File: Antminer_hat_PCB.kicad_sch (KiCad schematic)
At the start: 36 parts, among them J1 Conn_02x09_Odd_Even, J10 USB Expansion board, J11 Aux_mio_conn, J12 12v Pwr, J13 HDMI_A, J14 PL Pins, J2 Conn_02x09_Odd_Even, J3 Conn_02x09_Odd_Even, J4 Conn_02x09_Odd_Even, J5 Conn_02x09_Odd_Even, J6 Conn_02x09_Odd_Even, J7 Conn_02x09_Odd_Even, J8 Conn_02x09_Odd_Even, J9 Conn_02x09_Odd_Even, U1 L7805

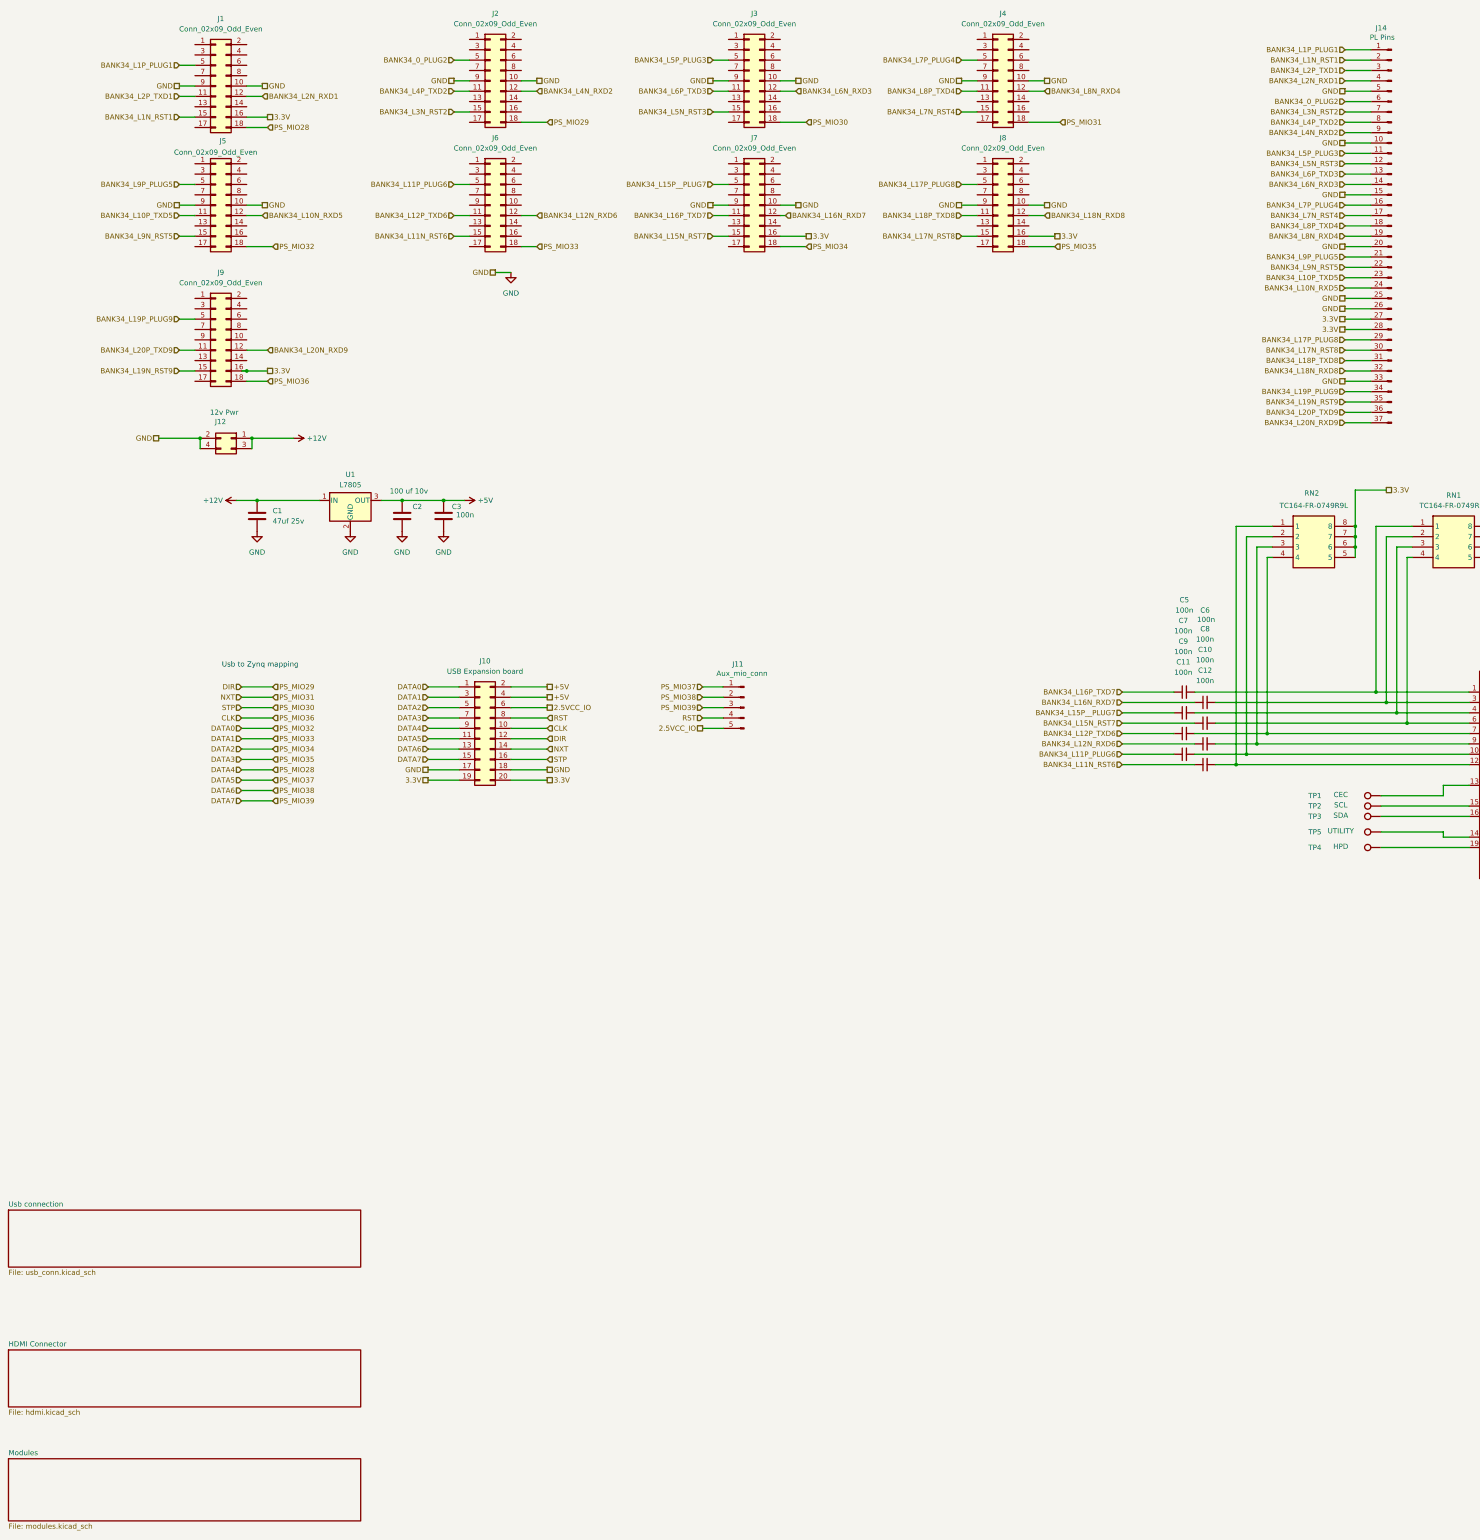
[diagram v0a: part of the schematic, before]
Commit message: Updates for version 1.1:  - Project named as Antminer_hat_pcb  - Added USB3315 Phy on board  - Removed ULPI connector  - Optimized HDMI wiring  - Other updates
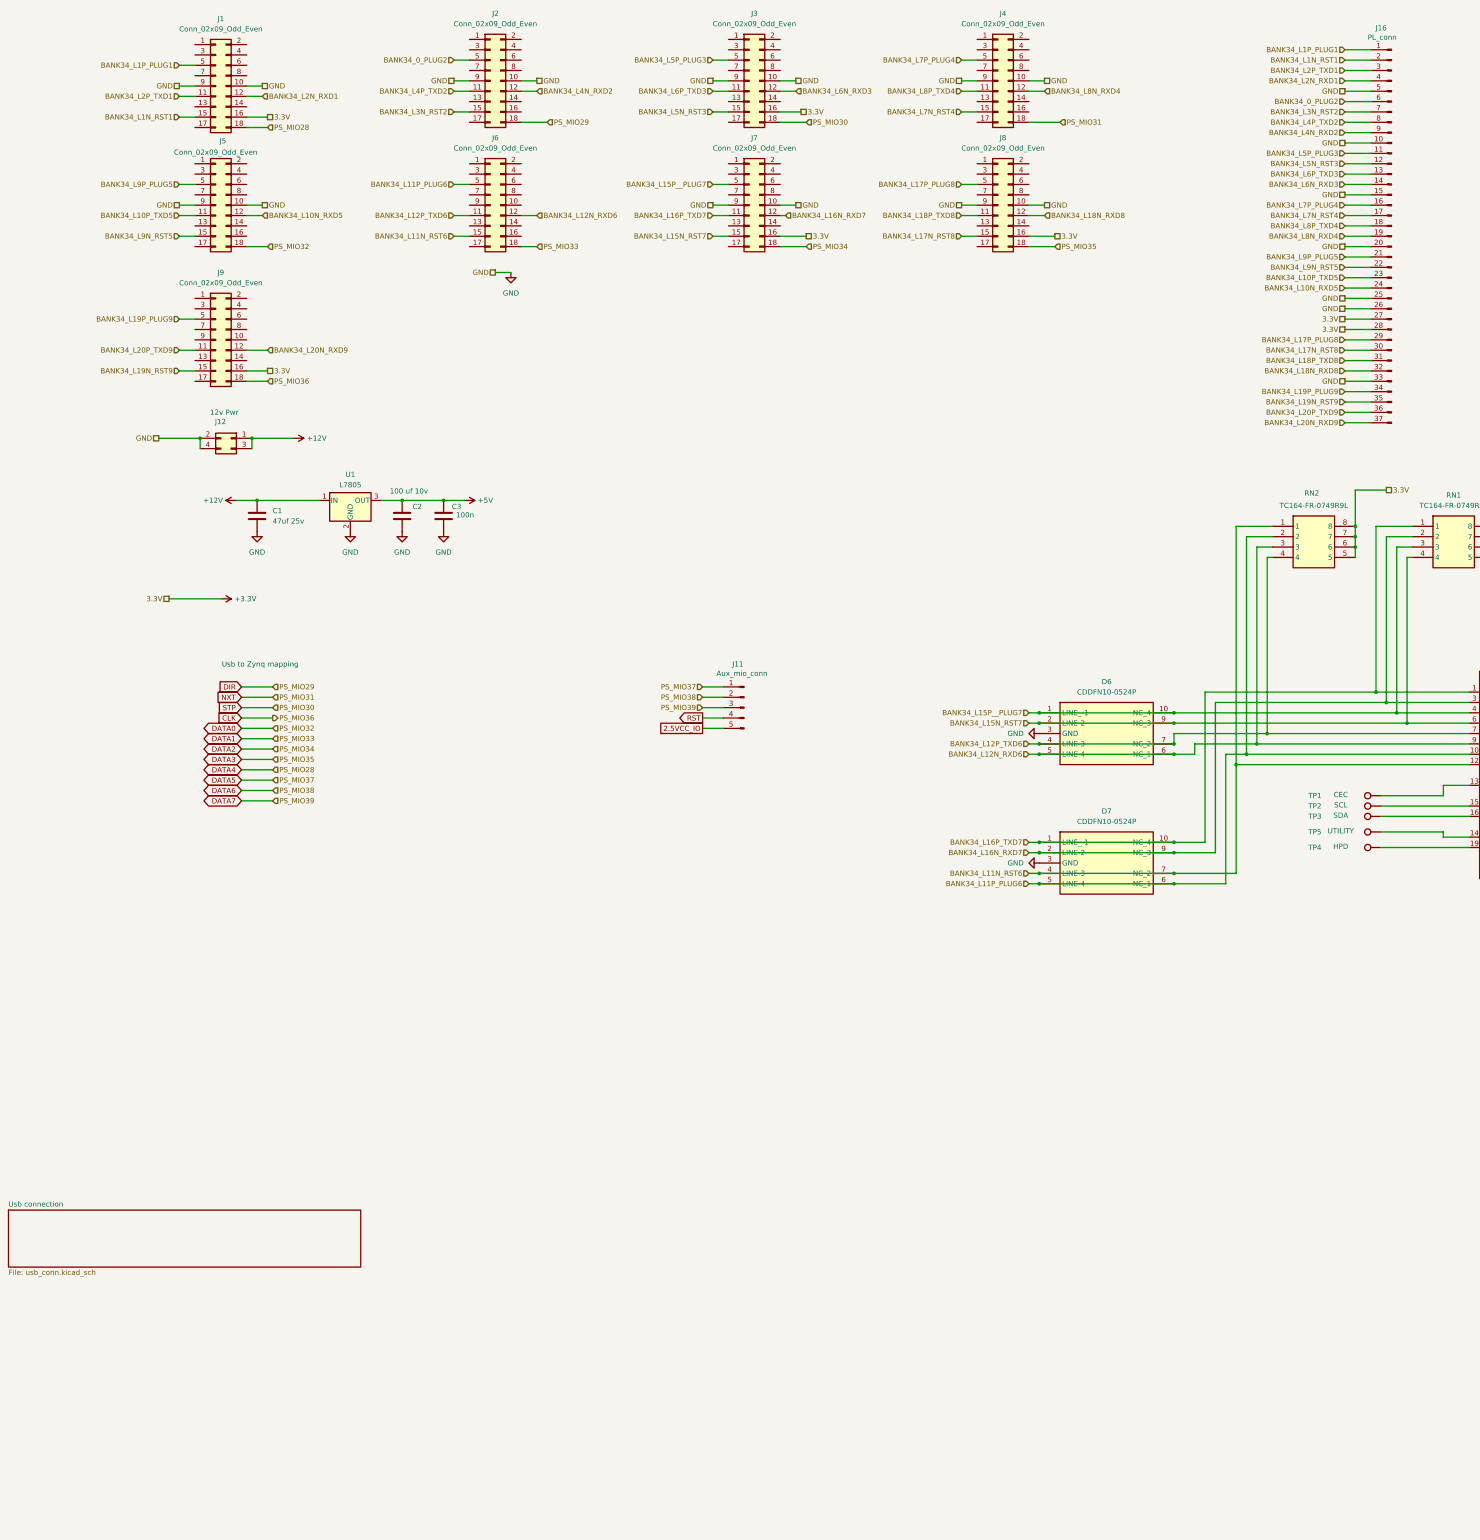
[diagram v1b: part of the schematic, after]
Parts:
- removed C10, C11, C12, C5, C6, C7, C8, C9: 100n, Capacitor_SMD:C_0603_1608Metric_Pad1.08x0.95mm_HandSolder, symbol Device:C_Small
- removed J10: USB Expansion board, Connector_PinSocket_2.54mm:PinSocket_2x10_P2.54mm_Horizontal, symbol Connector_Generic:Conn_02x10_Odd_Even
- added D6, D7: CDDFN10-0524P, SamacSys_Parts:CDDFN100524P, symbol SamacSys_Parts:CDDFN10-0524P
- J16: renamed from J14; value PL Pins -> PL_conn
- R1: footprint Resistor_SMD:R_1206_3216Metric -> Resistor_SMD:R_0805_2012Metric
- TP1, TP2, TP3, TP4, TP5, TP6: footprint TestPoint:TestPoint_Pad_D2.0mm -> TestPoint:TestPoint_Pad_D1.5mm
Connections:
- net 3.3V is gone; now on net +3.3V: J1.16 (Pin_16), J16.27 (Pin_27), J16.28 (Pin_28), J7.16 (Pin_16), J8.16 (Pin_16), J9.16 (Pin_16), RN1.5, RN1.6, RN1.7, RN1.8, RN2.5, RN2.6, RN2.7, RN2.8
- net BANK34_L11N_RST6: now also J13.12 (CK-), RN2.1, D7.4 (LINE-3), D7.7 (NC_2)
- net BANK34_L11P_PLUG6: now also J13.10 (CK+), RN2.2, D7.5 (LINE-4), D7.6 (NC_1)
- net BANK34_L12N_RXD6: now also J13.9 (D0-), RN2.3, D6.5 (LINE-4), D6.6 (NC_1)
- net BANK34_L12P_TXD6: now also J13.7 (D0+), RN2.4, D6.4 (LINE-3), D6.7 (NC_2)
- net BANK34_L15N_RST7: now also J13.6 (D1-), RN1.4, D6.2 (LINE-2), D6.9 (NC_3)
- net BANK34_L15P__PLUG7: now also J13.4 (D1+), RN1.3, D6.1 (LINE_-1), D6.10 (NC_4)
- net BANK34_L16N_RXD7: now also J13.3 (D2-), RN1.2, D7.2 (LINE-2), D7.9 (NC_3)
- net BANK34_L16P_TXD7: now also J13.1 (D2+), RN1.1, D7.1 (LINE_-1), D7.10 (NC_4)
- net GND: now also D6.3 (GND), D7.3 (GND)
- net +3.3V: now reaches J3.16 (Pin_16)
- net PS_MIO30 renamed STP
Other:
- removed sheet HDMI Connector
- removed sheet Modules
- title: KCC Tech S9 Board hat 2025 -> KCC Tech hat board for Antminer S9

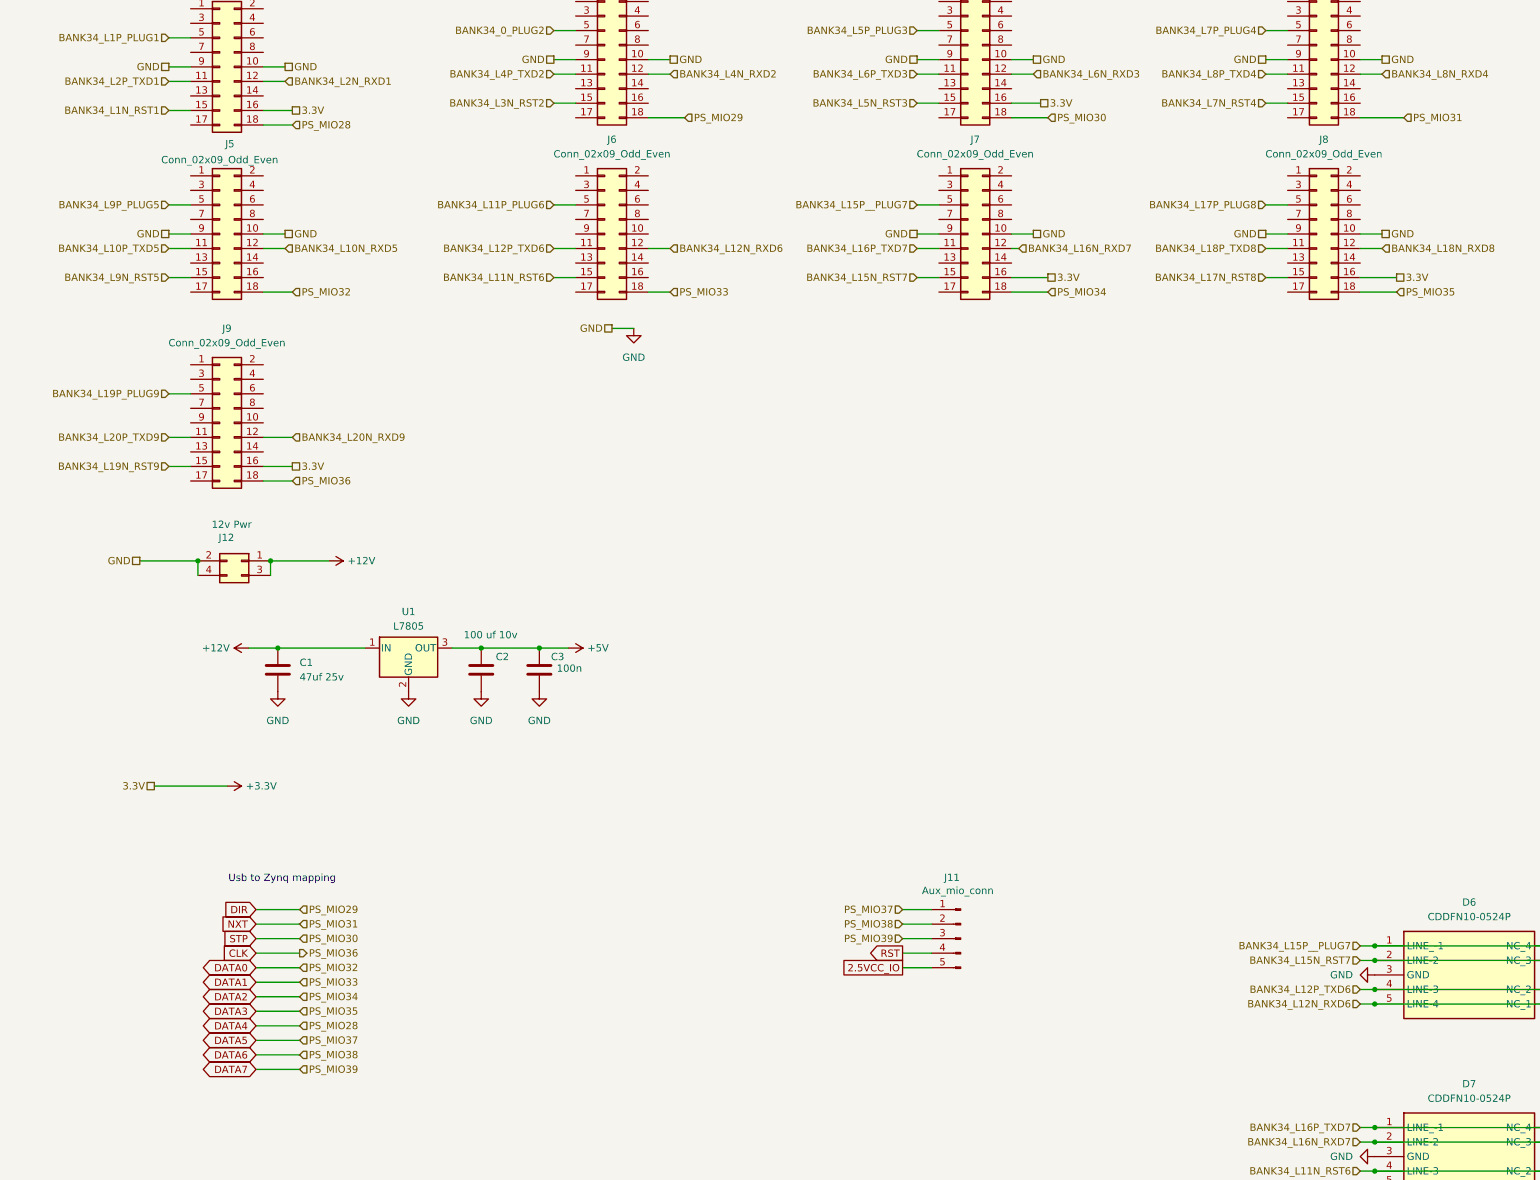
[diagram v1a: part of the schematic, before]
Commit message: - Updated schematic to use correct type of external connectors
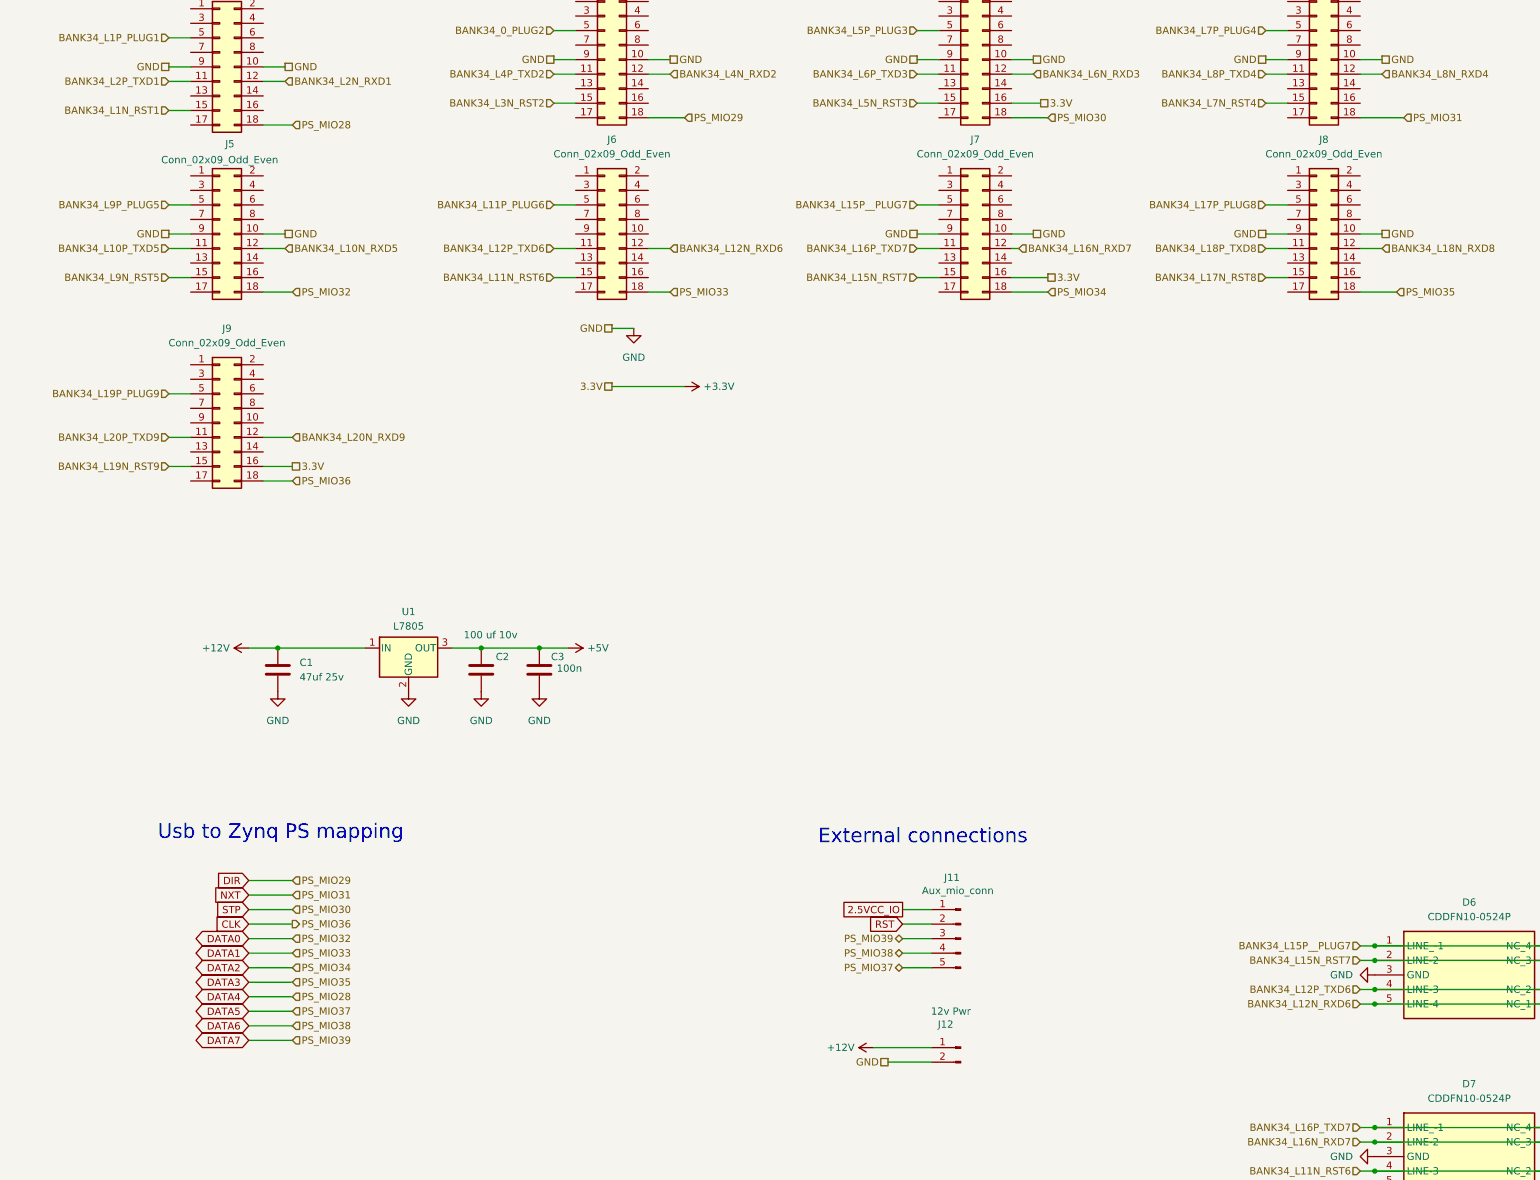
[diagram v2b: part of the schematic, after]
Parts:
- J11: footprint Connector_PinHeader_2.54mm:PinHeader_1x05_P2.54mm_Vertical -> Connector_PinHeader_2.54mm:PinHeader_1x05_P2.54mm_Horizontal
- J12: footprint Connector_PinSocket_2.54mm:PinSocket_2x02_P2.54mm_Vertical -> Connector_PinHeader_2.54mm:PinHeader_1x02_P2.54mm_Horizontal; symbol Connector_Generic:Conn_02x02_Odd_Even -> Connector:Conn_01x02_Pin
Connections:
- net +12V: no longer J12.3 (Pin_3)
- net +3.3V: no longer J1.16 (Pin_16), J8.16 (Pin_16)
- net 2.5VCC_IO: now also J11.1 (Pin_1); no longer J11.5 (Pin_5)
- net DATA5: now also J11.5 (Pin_5); no longer J11.1 (Pin_1)
- net DATA6: now also J11.4 (Pin_4); no longer J11.2 (Pin_2)
- net GND: no longer J12.4 (Pin_4)
- net RST: now also J11.2 (Pin_2); no longer J11.4 (Pin_4)
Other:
- note added: "External connections"
- note added: "Usb to Zynq PS mapping"
- note removed: "Usb to Zynq mapping"
